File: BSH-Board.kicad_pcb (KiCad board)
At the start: 2 copper layers, 20 x 35.5 mm, 69 parts, among them J1 667101210103, J2 MICRO QTZB5.0, Q1 MMST3904, SW1 TS-3025-B-C-B, SW2 TS-3025-B-C-B, U1 74LVC1G07, U2 74LVC1G17, U3 AP63203WU, U4 ESP32-C6-MINI-1-N4

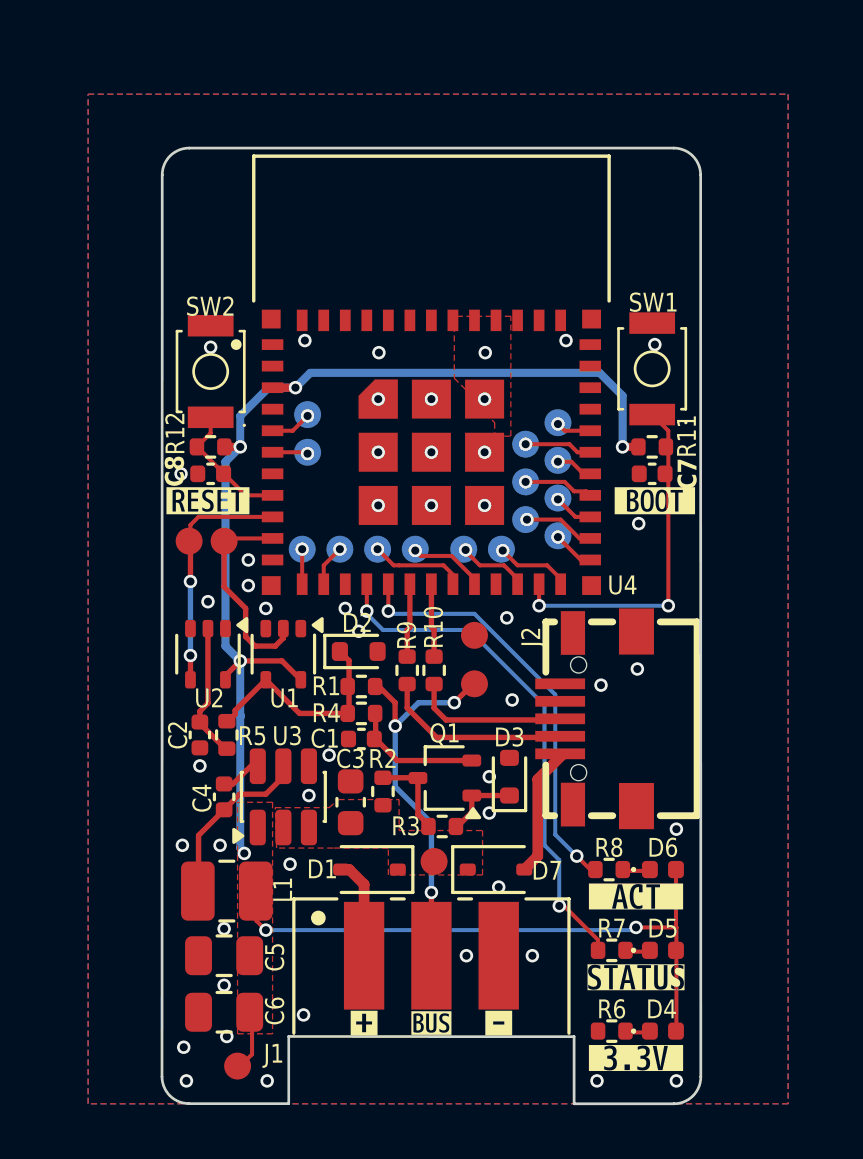
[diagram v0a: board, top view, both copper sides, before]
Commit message: V1.0 with antenna cutout
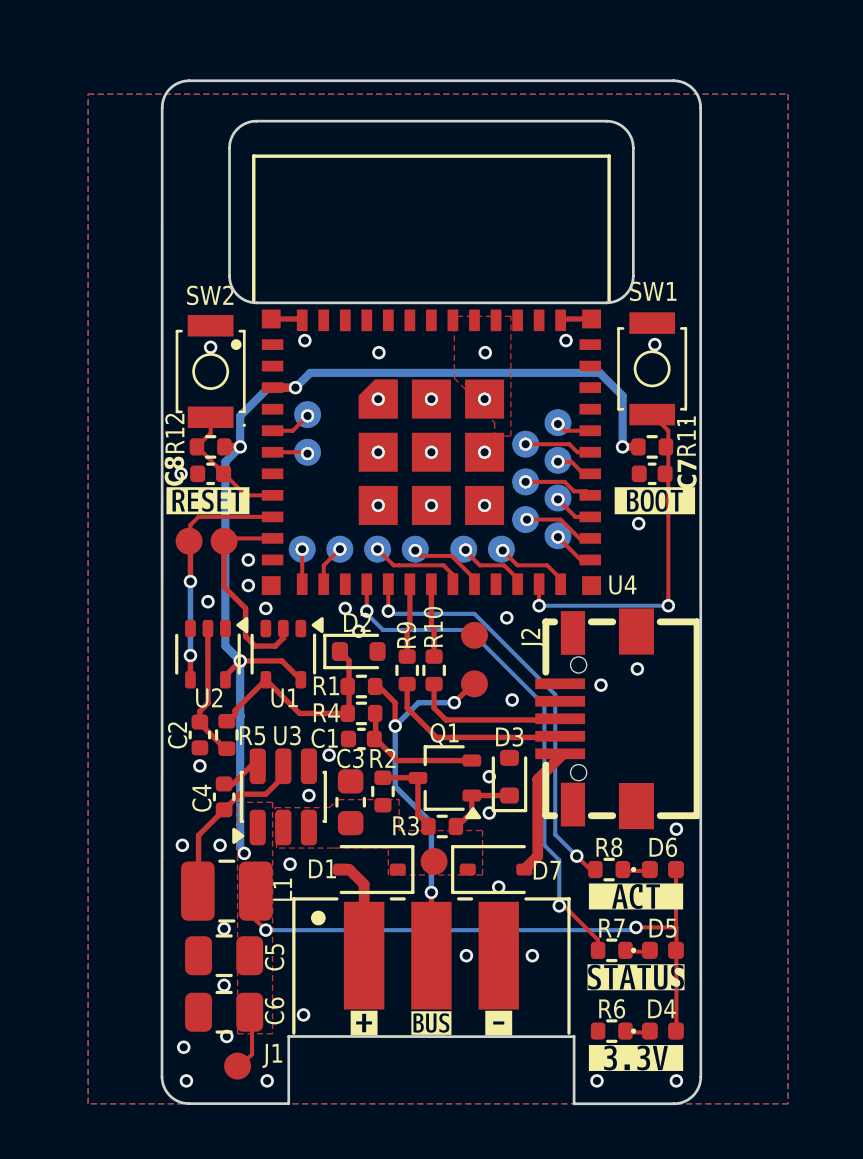
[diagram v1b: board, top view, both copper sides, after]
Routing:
- net GND: track 0.00 -> 2.34 mm
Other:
- board size 20 x 35.5 mm -> 20 x 38 mm
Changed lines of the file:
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@@
 		(tags "SW-SMD_L3.0-W2.5-P3.40-LS4.0-L footprint C2689695")
 		(property "Reference" "SW1"
-			(at 2.45 0.05 180)
+			(at 2.85 0.05 180)
 			(layer "F.SilkS")
 			(effects
@@
 		(tags "SW-SMD_L3.0-W2.5-P3.40-LS4.0-L footprint C2689695")
 		(property "Reference" "SW2"
-			(at 2.4 0 180)
+			(at 2.8 0 180)
 			(layer "F.SilkS")
 			(effects
@@
 	)
 	(gr_line
-		(start 113 55.5)
-		(end 131 55.5)
+		(start 114.5 55.5)
+		(end 114.5 60.25)
 		(stroke
 			(width 0.1)
@@
 	)
 	(gr_line
+		(start 113 53)
+		(end 131 53)
+		(stroke
+			(width 0.1)
+			(type default)
+		)
+		(layer "Edge.Cuts")
+	)
+	(gr_line
 		(start 116.7 90.992893)
 		(end 112.992893 90.992893)
@@
 	)
 	(gr_line
+		(start 115.5 54.5)
+		(end 128.5 54.5)
+		(stroke
+			(width 0.1)
+			(type solid)
+		)
+		(layer "Edge.Cuts")
+	)
+	(gr_line
 		(start 127.3 91)
 		(end 131.007107 91)
@@
 	)
 	(gr_arc
-		(start 131 55.5)
-		(mid 131.707107 55.792893)
-		(end 132 56.5)
+		(start 131 53)
+		(mid 131.707107 53.292893)
+		(end 132 54)
+		(stroke
+			(width 0.1)
+			(type default)
+		)
+		(layer "Edge.Cuts")
+	)
+	(gr_arc
+		(start 129.5 60.25)
+		(mid 129.207107 60.957107)
+		(end 128.5 61.25)
+		(stroke
+			(width 0.1)
+			(type default)
+		)
+		(layer "Edge.Cuts")
+	)
+	(gr_line
+		(start 128.5 61.25)
+		(end 115.5 61.25)
 		(stroke
 			(width 0.1)
@@
 	)
 	(gr_line
-		(start 132 56.5)
+		(start 132 54)
 		(end 132.007107 90)
 		(stroke
@@
 		(layer "Edge.Cuts")
 	)
+	(gr_arc
+		(start 115.5 61.25)
+		(mid 114.792893 60.957107)
+		(end 114.5 60.25)
+		(stroke
+			(width 0.1)
+			(type default)
+		)
+		(layer "Edge.Cuts")
+	)
 	(gr_line
 		(start 111.992893 89.992893)
-		(end 112.001103 56.5)
+		(end 112 54)
 		(stroke
 			(width 0.1)
@@
 		(layer "Edge.Cuts")
 	)
+	(gr_line
+		(start 129.5 55.5)
+		(end 129.5 60.25)
+		(stroke
+			(width 0.1)
+			(type default)
+		)
+		(layer "Edge.Cuts")
+	)
 	(gr_arc
-		(start 112 56.5)
-		(mid 112.292893 55.792893)
-		(end 113 55.5)
+		(start 112 54)
+		(mid 112.292893 53.292893)
+		(end 113 53)
+		(stroke
+			(width 0.1)
+			(type default)
+		)
+		(layer "Edge.Cuts")
+	)
+	(gr_arc
+		(start 114.5 55.5)
+		(mid 114.792893 54.792893)
+		(end 115.5 54.5)
+		(stroke
+			(width 0.1)
+			(type default)
+		)
+		(layer "Edge.Cuts")
+	)
+	(gr_arc
+		(start 128.5 54.5)
+		(mid 129.207107 54.792893)
+		(end 129.5 55.5)
 		(stroke
 			(width 0.1)
@@
 		)
 	)
+	(segment
+		(start 117.15 61.85)
+		(end 117.2 61.9)
+		(width 0.2)
+		(layer "F.Cu")
+		(net 2)
+	)
+	(segment
+		(start 126.85 61.85)
+		(end 126.8 61.9)
+		(width 0.2)
+		(layer "F.Cu")
+		(net 2)
+	)
+	(segment
+		(start 127.95 61.85)
+		(end 126.85 61.85)
+		(width 0.2)
+		(layer "F.Cu")
+		(net 2)
+	)
+	(segment
+		(start 116.05 61.85)
+		(end 117.15 61.85)
+		(width 0.2)
+		(layer "F.Cu")
+		(net 2)
+	)
 	(via
 		(at 124.15 78.85)
@@
 		(polygon
 			(pts
-				(xy 112 55.5) (xy 132 55.5) (xy 132 61.25) (xy 112 61.25)
+				(xy 112 53) (xy 132 53) (xy 132 61.25) (xy 112 61.25)
 			)
 		)

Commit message: Add RAST coding notch
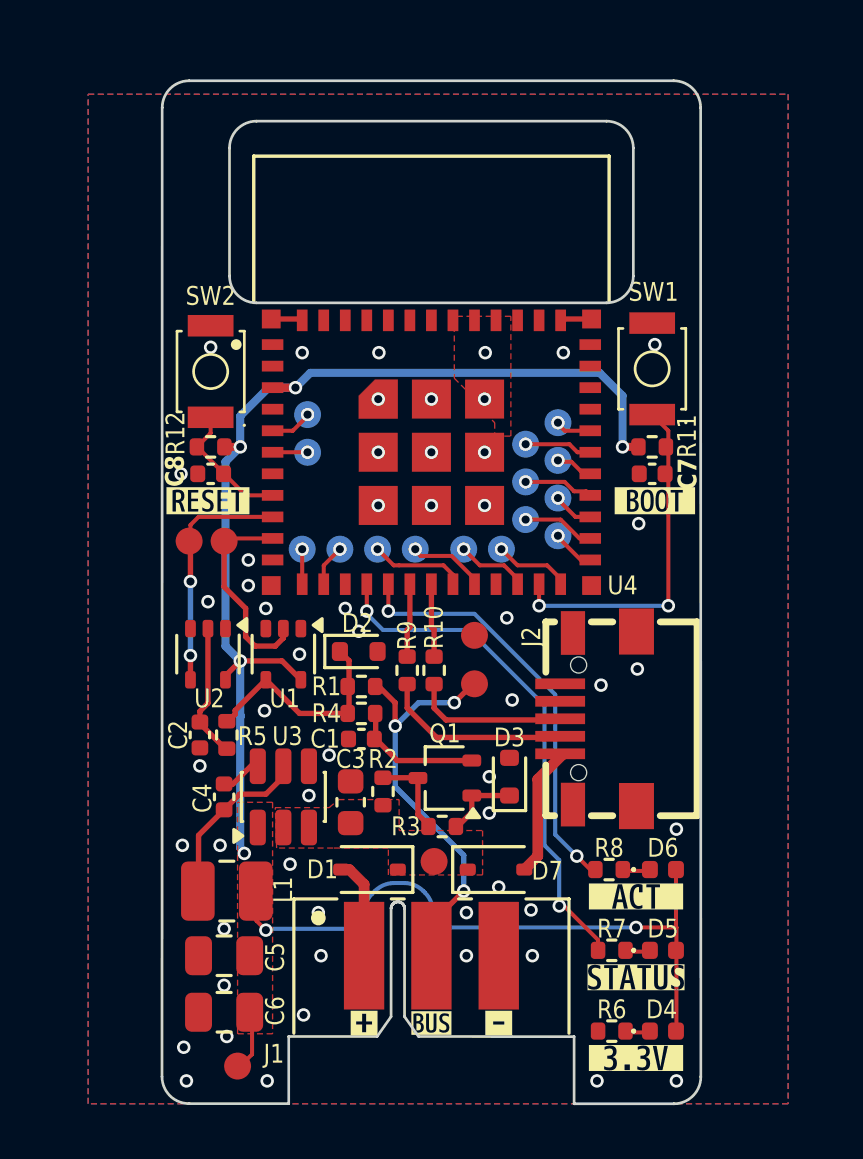
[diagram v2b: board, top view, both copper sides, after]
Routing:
- net +3.3V: track 64.6 -> 66.6 mm
- net Net-(J1-PadA2): track 14.5 -> 15.5 mm
- net GND: vias 48 -> 54
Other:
- outline, holes or cut-outs redrawn

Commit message: Add dip switch for pullup, add TX pullup, add empty 0805 for potential other pullup value
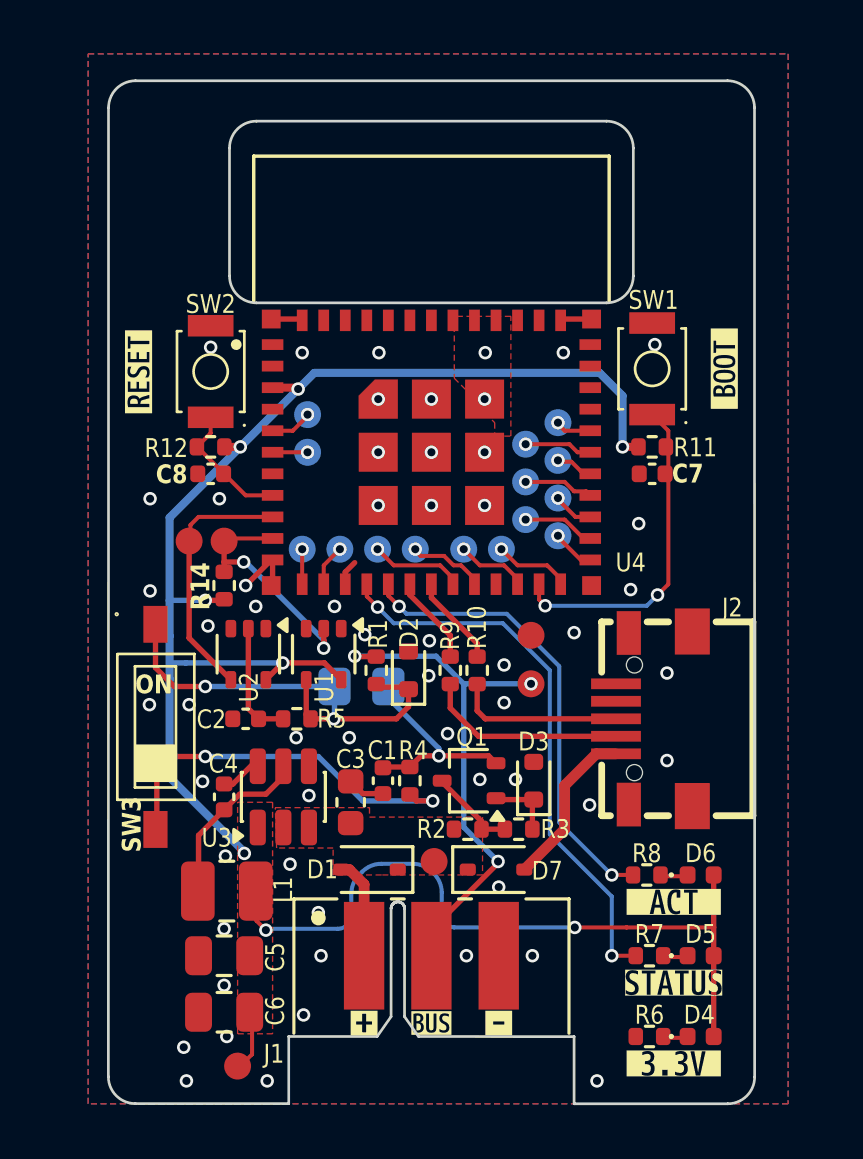
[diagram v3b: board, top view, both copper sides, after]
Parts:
- added R13: ?k, Resistor_SMD:R_0805_2012Metric_Pad1.20x1.40mm_HandSolder, B.Cu at (119.4, 75.5)
- added R14: 10k, Resistor_SMD:R_0402_1005Metric, F.Cu at (114.3, 71.8)
- added SW3: SW_DIP_x01, footprints:SW-SMD_DSHP01TSGER, F.Cu at (111.8, 77.0)
- moved kibuzzard-695BD459 5.54 mm to (132.9, 63.7), turned to 90 degrees
- moved kibuzzard-695BD43C 5.44 mm to (111.1, 63.8), turned to 90 degrees
- moved R2 3.45 mm to (123.3, 80.8), turned to 180 degrees
- moved R4 3.08 mm to (121.2, 79.0), turned to 90 degrees
- moved R3 2.84 mm to (125.2, 80.8)
- moved R5 2.67 mm to (117.0, 76.7), turned to 0 degrees
- moved TP1 2.10 mm to (125.7, 73.6)
- moved TP2 2.10 mm to (125.7, 75.4)
- moved J2 2.07 mm to (130.3, 76.7)
- moved D2 1.98 mm to (121.2, 74.9), turned to 90 degrees
- moved C2 1.80 mm to (115.1, 76.7), turned to 0 degrees
- moved C1 1.74 mm to (120.2, 79.0), turned to 90 degrees
- moved R10 1.60 mm to (123.7, 74.9)
- moved R9 1.60 mm to (122.7, 74.9)
- moved U1 1.50 mm to (118.0, 74.3)
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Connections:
- R4 pad 1: Net-(D2-K) -> Net-(R4-Pad1)
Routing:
- net Net-(R4-Pad1): track 0.00 -> 14.2 mm, vias 0 -> 2
- net +3.3V: track 66.6 -> 76.5 mm, vias 7 -> 8
- net Net-(D2-K): track 8.12 -> 17.0 mm, vias 0 -> 2
- net GND: track 2.34 -> 7.04 mm, vias 54 -> 57
- net Net-(J1-PadA2): track 15.5 -> 19.5 mm
- net Net-(Q1-E): track 4.86 -> 7.99 mm, vias 0 -> 1
- net STATUS: track 19.2 -> 20.8 mm
- net ACTIVITY: track 15.7 -> 17.4 mm
- net Net-(D7-A): track 4.85 -> 6.14 mm
- net DBUS-TX: track 7.66 -> 8.88 mm, vias 0 -> 2
- net DBUS-RX: track 8.84 -> 9.52 mm, vias 2 -> 0
- net Net-(C2-Pad2): track 5.05 -> 4.42 mm
- net Net-(U4-IO13): track 2.78 -> 3.39 mm
- net BOOT: track 12.9 -> 12.3 mm
- net Net-(U4-IO12): track 2.78 -> 3.31 mm
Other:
- board size 20 x 38 mm -> 24 x 38 mm

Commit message: Various minor improvements
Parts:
- removed kibuzzard-695BD43C: G***, kibuzzard-695BD43C
- removed kibuzzard-695BD459: G***, kibuzzard-695BD459
- removed kibuzzard-695C20AA: G***, kibuzzard-695C20AA
- removed kibuzzard-695C20B0: G***, kibuzzard-695C20B0
- removed kibuzzard-695C20DE: G***, kibuzzard-695C20DE
- removed kibuzzard-695CB6D3 (x2): G***, kibuzzard-695CB6D3
- removed kibuzzard-695CB704 (x2): G***, kibuzzard-695CB704
- removed kibuzzard-695CB724 (x2): G***, kibuzzard-695CB724
- added kibuzzard-69A53AD7: G***, kibuzzard-69A53AD7, F.Cu at (112.6, 64.8)
- added kibuzzard-69A53AE7: G***, kibuzzard-69A53AE7, F.Cu at (131.4, 64.7)
- added kibuzzard-69A53B23: G***, kibuzzard-69A53B23, F.Cu at (131.0, 86.6)
- added kibuzzard-69A53B53: G***, kibuzzard-69A53B53, F.Cu at (131.0, 89.7)
- added kibuzzard-69A53B6F: G***, kibuzzard-69A53B6F, F.Cu at (131.0, 83.6)
- added kibuzzard-69A53BB2: G***, kibuzzard-69A53BB2, F.Cu at (126.1, 87.7)
- added kibuzzard-69A53BB2: G***, kibuzzard-69A53BB2, B.Cu at (117.9, 87.7)
- added kibuzzard-69A53BC4: G***, kibuzzard-69A53BC4, F.Cu at (117.9, 87.7)
- added kibuzzard-69A53BC4: G***, kibuzzard-69A53BC4, B.Cu at (126.1, 87.7)
- added kibuzzard-69A53BD0: G***, kibuzzard-69A53BD0, F.Cu at (122.0, 88.0)
- added kibuzzard-69A53BD0: G***, kibuzzard-69A53BD0, B.Cu at (122.0, 88.0)
- added kibuzzard-69A53C55: G***, kibuzzard-69A53C55, F.Cu at (110.6, 81.8)
- moved R11 5.06 mm to (132.3, 71.2), turned to -90 degrees
- moved R12 5.06 mm to (111.7, 71.2), turned to -90 degrees
- moved SW1 3.38 mm to (131.3, 66.9), turned to 0 degrees
- moved SW2 3.29 mm to (112.7, 66.9), turned to 180 degrees
- moved C7 2.70 mm to (132.3, 69.3), turned to 90 degrees
- moved C8 2.70 mm to (111.7, 69.3), turned to 90 degrees
- moved J2 0.07 mm to (130.2, 76.7)
- moved D2 0.05 mm to (121.1, 74.9)
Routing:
- net +3.3V: track 76.5 -> 71.6 mm, vias 8 -> 7
- net RESET: track 4.87 -> 7.87 mm
- net BOOT: track 12.3 -> 13.2 mm
- net GND: vias 57 -> 53
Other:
- board size 24 x 38 mm -> 28 x 38 mm
- board text added: "V-Cut"

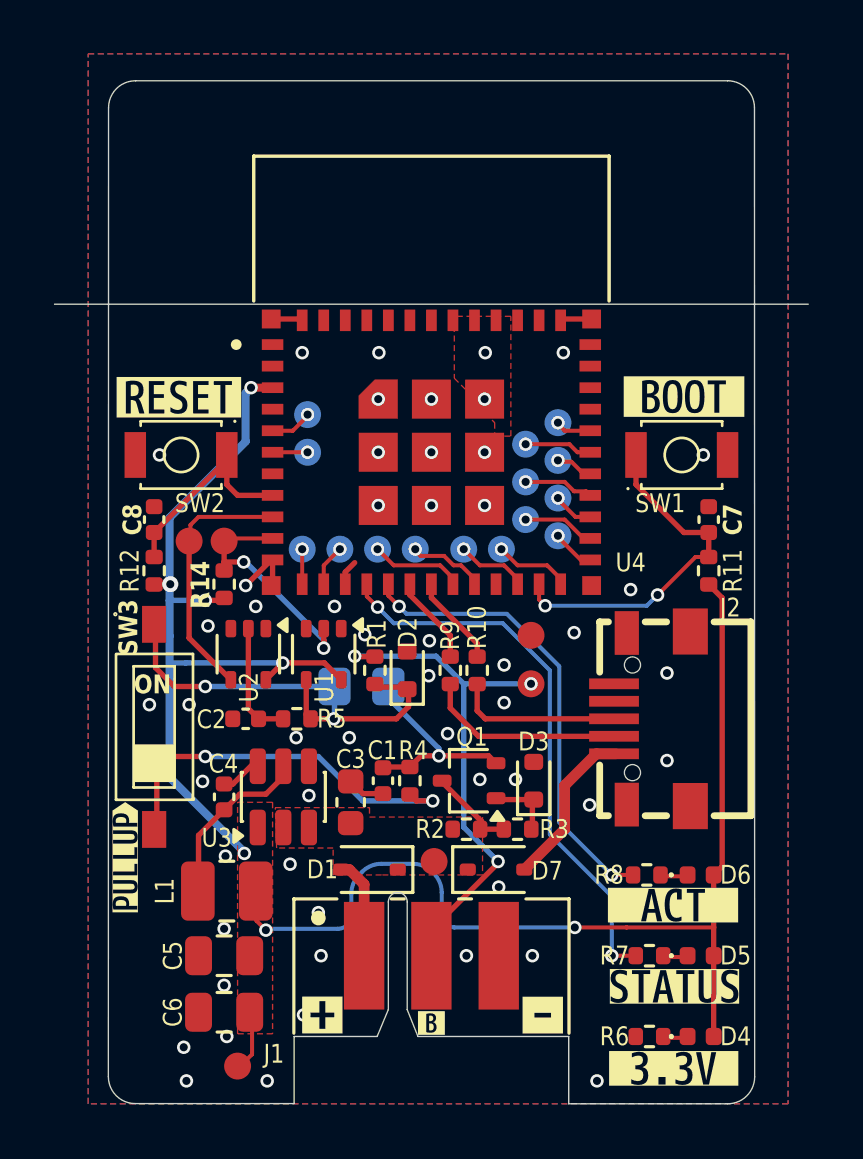
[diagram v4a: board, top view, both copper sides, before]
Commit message: Put V-Cut into seperate layer
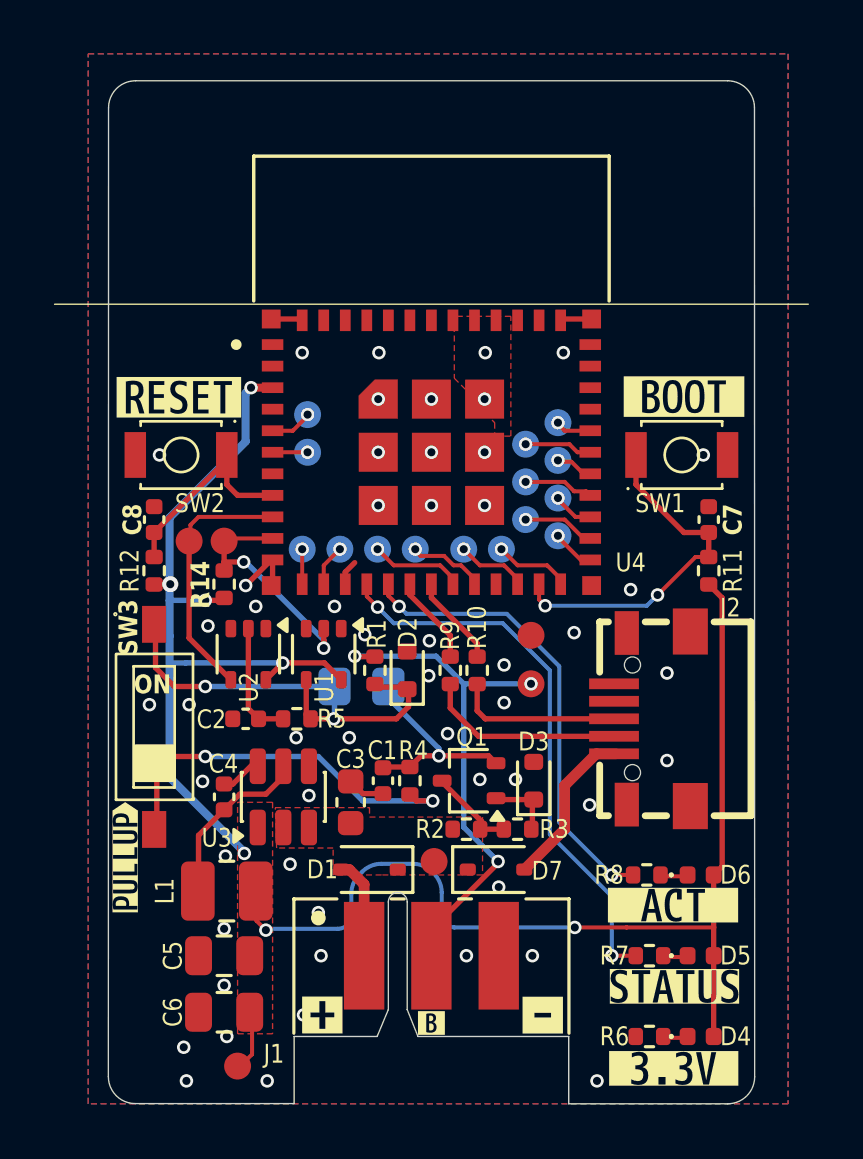
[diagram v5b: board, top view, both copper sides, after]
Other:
- board size 28 x 38 mm -> 24 x 38 mm
- board text removed: "V-Cut"
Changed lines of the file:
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@@
 		(41 "User.2" user)
 		(43 "User.3" user)
-		(45 "User.4" user)
+		(45 "User.4" user "V-Cuts")
 	)
 	(setup
@@
 		(embedded_fonts no)
 	)
+	(gr_line
+		(start 108 61.3)
+		(end 136 61.3)
+		(stroke
+			(width 0.05)
+			(type solid)
+		)
+		(layer "F.SilkS")
+	)
+	(gr_line
+		(start 108 61.3)
+		(end 136 61.3)
+		(stroke
+			(width 0.05)
+			(type solid)
+		)
+		(layer "B.SilkS")
+	)
 	(gr_arc
 		(start 134.007107 90)
@@
 	)
 	(gr_line
-		(start 108 61.3)
-		(end 136 61.3)
-		(stroke
-			(width 0.05)
-			(type solid)
-		)
-		(layer "Edge.Cuts")
-	)
-	(gr_line
 		(start 116.9 88.5)
 		(end 119.983084 88.5)
@@
 		(layer "User.2")
 	)
+	(gr_line
+		(start 108 61.3)
+		(end 136 61.3)
+		(stroke
+			(width 0.05)
+			(type solid)
+		)
+		(layer "User.4")
+	)
 	(gr_text "23"
 		(at 128.4 67.6 0)
@@
 		)
 	)
-	(gr_text "V-Cut"
-		(at 136 61.9 0)
-		(layer "Edge.Cuts")
-		(effects
-			(font
-				(size 1 1)
-				(thickness 0.15)
-			)
-			(justify left bottom)
-		)
-	)
 	(dimension
 		(type orthogonal)
@@
 			(effects
 				(font
-					(size 1 1)
-					(thickness 0.15)
-				)
-			)
-		)
-	)
-	(dimension
-		(type orthogonal)
-		(layer "User.4")
-		(pts
-			(xy 110 53.975) (xy 134 53.975)
-		)
-		(height -3.85)
-		(orientation 0)
-		(format
-			(prefix "")
-			(suffix "")
-			(units 3)
-			(units_format 0)
-			(precision 4)
-			(suppress_zeroes yes)
-		)
-		(style
-			(thickness 0.1)
-			(arrow_length 1.27)
-			(text_position_mode 0)
-			(arrow_direction outward)
-			(extension_height 0.58642)
-			(extension_offset 0.5)
-			(keep_text_aligned yes)
-		)
-		(gr_text "24"
-			(at 122 48.975 0)
-			(layer "User.4")
-			(effects
-				(font
-					(size 1 1)
-					(thickness 0.15)
-				)
-			)
-		)
-	)
-	(dimension
-		(type orthogonal)
-		(layer "User.4")
-		(pts
-			(xy 133 91) (xy 133 53)
-		)
-		(height 6.75)
-		(orientation 1)
-		(format
-			(prefix "")
-			(suffix "")
-			(units 3)
-			(units_format 0)
-			(precision 4)
-			(suppress_zeroes yes)
-		)
-		(style
-			(thickness 0.1)
-			(arrow_length 1.27)
-			(text_position_mode 0)
-			(arrow_direction outward)
-			(extension_height 0.58642)
-			(extension_offset 0.5)
-			(keep_text_aligned yes)
-		)
-		(gr_text "38"
-			(at 138.6 72 90)
-			(layer "User.4")
-			(effects
-				(font
